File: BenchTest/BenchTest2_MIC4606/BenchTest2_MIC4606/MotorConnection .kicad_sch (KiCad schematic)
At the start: 4 parts, among them J1 Conn_01x01_Socket, J3 Conn_01x01_Socket, J4 Conn_01x01_Socket, J5 Conn_01x01_Socket

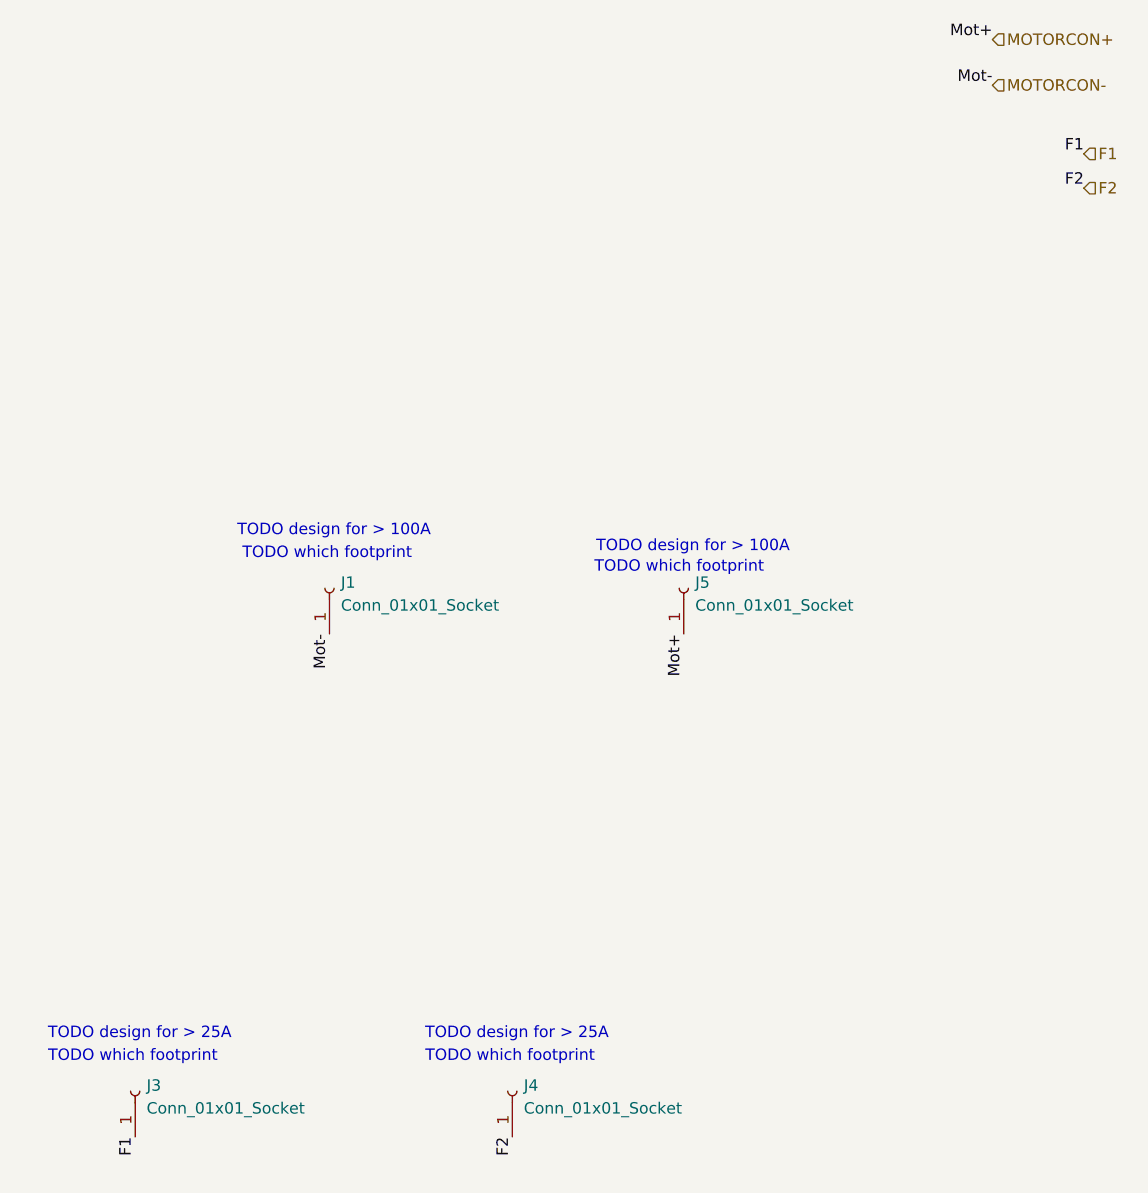
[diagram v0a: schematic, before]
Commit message: Assigned HP Footprints
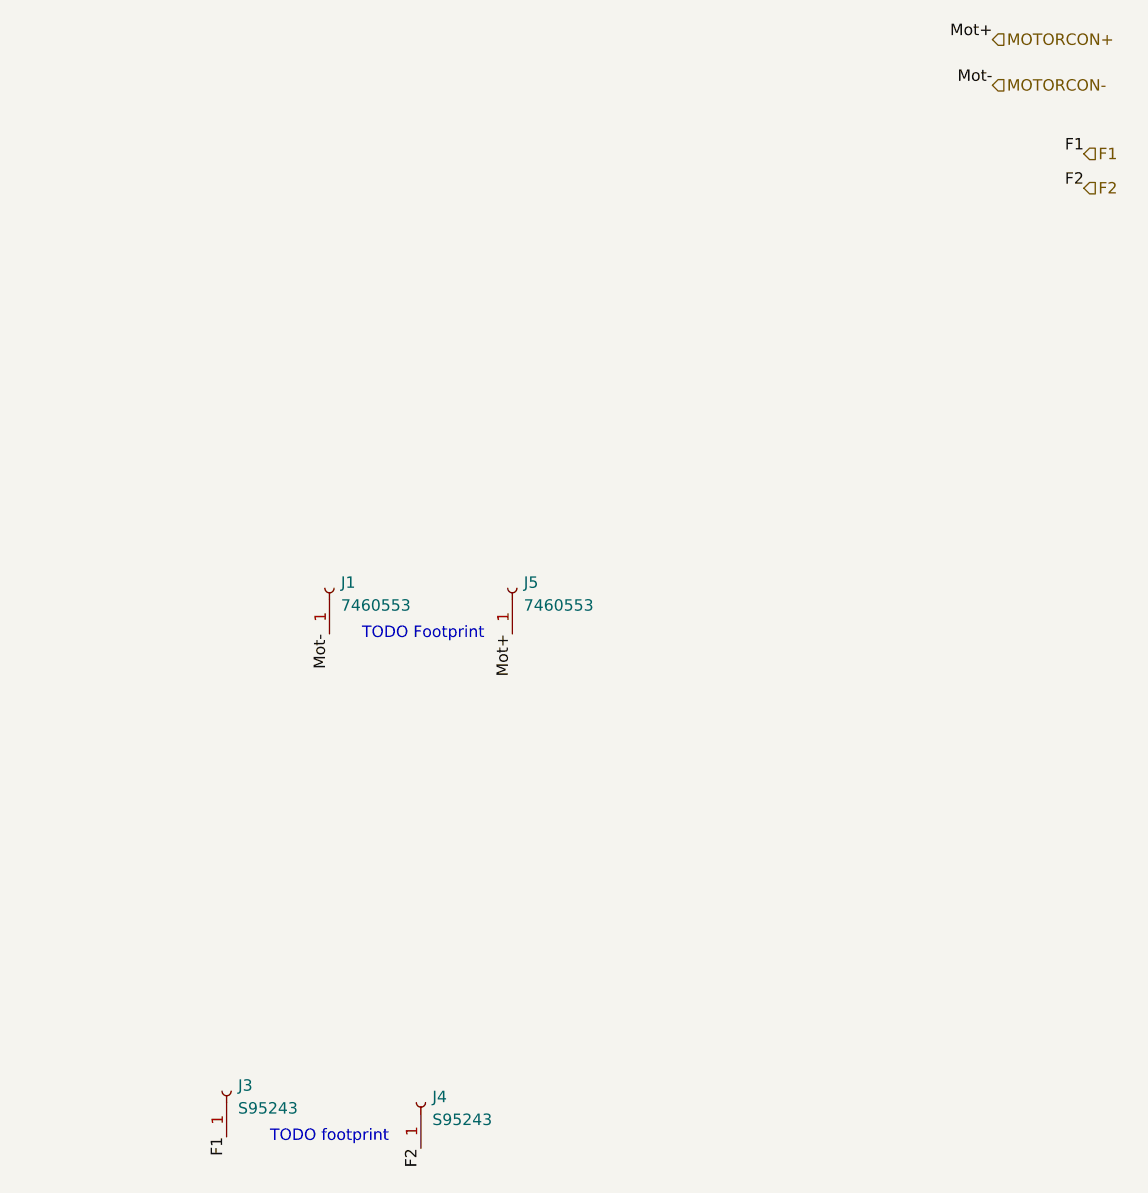
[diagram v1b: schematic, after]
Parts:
- J1, J5: value Conn_01x01_Socket -> 7460553
- J3, J4: value Conn_01x01_Socket -> S95243
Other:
- note added: "TODO Footprint"
- note added: "TODO footprint"
- note removed: "TODO design for > 100A"
- note removed: "TODO design for > 25A"
- note removed: "TODO which footprint"
- moved on the sheet: J3, J4, J5
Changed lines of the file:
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@@
 	(generator_version "9.0")
 	(paper "A4")
-	(text "TODO which footprint"
-		(exclude_from_sim no)
-		(at 173.736 132.08 0)
-		(effects
-			(font
-				(size 1.27 1.27)
-			)
-		)
-	)
-	(text "TODO which footprint"
-		(exclude_from_sim no)
-		(at 195.326 76.2 0)
-		(effects
-			(font
-				(size 1.27 1.27)
-			)
-		)
-	)
-	(text "TODO which footprint"
-		(exclude_from_sim no)
-		(at 234.442 77.724 0)
-		(effects
-			(font
-				(size 1.27 1.27)
-			)
-		)
-	)
-	(text "TODO design for > 100A"
-		(exclude_from_sim no)
-		(at 235.966 75.438 0)
-		(effects
-			(font
-				(size 1.27 1.27)
-			)
-		)
-	)
-	(text "TODO which footprint"
-		(exclude_from_sim no)
-		(at 215.646 132.08 0)
-		(effects
-			(font
-				(size 1.27 1.27)
-			)
-		)
-	)
-	(text "TODO design for > 100A"
-		(exclude_from_sim no)
-		(at 196.088 73.66 0)
-		(effects
-			(font
-				(size 1.27 1.27)
-			)
-		)
-	)
-	(text "TODO design for > 25A"
-		(exclude_from_sim no)
-		(at 216.408 129.54 0)
-		(effects
-			(font
-				(size 1.27 1.27)
-			)
-		)
-	)
-	(text "TODO design for > 25A"
-		(exclude_from_sim no)
-		(at 174.498 129.54 0)
+	(text "TODO Footprint"
+		(exclude_from_sim no)
+		(at 205.994 85.09 0)
+		(effects
+			(font
+				(size 1.27 1.27)
+			)
+		)
+	)
+	(text "TODO footprint"
+		(exclude_from_sim no)
+		(at 195.58 140.97 0)
 		(effects
 			(font
@@
 	)
 	(label "Mot+"
-		(at 234.95 85.09 270)
+		(at 215.9 85.09 270)
 		(effects
 			(font
@@
 	)
 	(label "F1"
-		(at 173.99 140.97 270)
+		(at 184.15 140.97 270)
 		(effects
 			(font
@@
 	)
 	(label "F2"
-		(at 215.9 140.97 270)
+		(at 205.74 142.24 270)
 		(effects
 			(font
@@
 			)
 		)
-		(property "Value" "Conn_01x01_Socket"
+		(property "Value" "7460553"
 			(at 196.85 81.9149 90)
 			(effects
@@
 			)
 		)
-		(property "Description" "Generic connector, single row, 01x01, script generated"
+		(property "Description" "7460553"
 			(at 195.58 80.01 0)
 			(effects
@@
 	(symbol
 		(lib_id "Connector:Conn_01x01_Socket")
-		(at 173.99 135.89 90)
+		(at 184.15 135.89 90)
 		(unit 1)
 		(exclude_from_sim no)
@@
 		(fields_autoplaced yes)
 		(property "Reference" "J3"
-			(at 175.26 135.2549 90)
-			(effects
-				(font
-					(size 1.27 1.27)
-				)
-				(justify right)
-			)
-		)
-		(property "Value" "Conn_01x01_Socket"
-			(at 175.26 137.7949 90)
+			(at 185.42 135.2549 90)
+			(effects
+				(font
+					(size 1.27 1.27)
+				)
+				(justify right)
+			)
+		)
+		(property "Value" "S95243"
+			(at 185.42 137.7949 90)
 			(effects
 				(font
@@
 		)
 		(property "Footprint" ""
-			(at 173.99 135.89 0)
+			(at 184.15 135.89 0)
 			(effects
 				(font
@@
 		)
 		(property "Datasheet" "~"
-			(at 173.99 135.89 0)
-			(effects
-				(font
-					(size 1.27 1.27)
-				)
-				(hide yes)
-			)
-		)
-		(property "Description" "Generic connector, single row, 01x01, script generated"
-			(at 173.99 135.89 0)
+			(at 184.15 135.89 0)
+			(effects
+				(font
+					(size 1.27 1.27)
+				)
+				(hide yes)
+			)
+		)
+		(property "Description" "S95243"
+			(at 184.15 135.89 0)
 			(effects
 				(font
@@
 	(symbol
 		(lib_id "Connector:Conn_01x01_Socket")
-		(at 234.95 80.01 90)
+		(at 215.9 80.01 90)
 		(unit 1)
 		(exclude_from_sim no)
@@
 		(fields_autoplaced yes)
 		(property "Reference" "J5"
-			(at 236.22 79.3749 90)
-			(effects
-				(font
-					(size 1.27 1.27)
-				)
-				(justify right)
-			)
-		)
-		(property "Value" "Conn_01x01_Socket"
-			(at 236.22 81.9149 90)
+			(at 217.17 79.3749 90)
+			(effects
+				(font
+					(size 1.27 1.27)
+				)
+				(justify right)
+			)
+		)
+		(property "Value" "7460553"
+			(at 217.17 81.9149 90)
 			(effects
 				(font
@@
 		)
 		(property "Footprint" ""
-			(at 234.95 80.01 0)
+			(at 215.9 80.01 0)
 			(effects
 				(font
@@
 		)
 		(property "Datasheet" "~"
-			(at 234.95 80.01 0)
-			(effects
-				(font
-					(size 1.27 1.27)
-				)
-				(hide yes)
-			)
-		)
-		(property "Description" "Generic connector, single row, 01x01, script generated"
-			(at 234.95 80.01 0)
+			(at 215.9 80.01 0)
+			(effects
+				(font
+					(size 1.27 1.27)
+				)
+				(hide yes)
+			)
+		)
+		(property "Description" "7460553"
+			(at 215.9 80.01 0)
 			(effects
 				(font
@@
 	(symbol
 		(lib_id "Connector:Conn_01x01_Socket")
-		(at 215.9 135.89 90)
+		(at 205.74 137.16 90)
 		(unit 1)
 		(exclude_from_sim no)
@@
 		(fields_autoplaced yes)
 		(property "Reference" "J4"
-			(at 217.17 135.2549 90)
-			(effects
-				(font
-					(size 1.27 1.27)
-				)
-				(justify right)
-			)
-		)
-		(property "Value" "Conn_01x01_Socket"
-			(at 217.17 137.7949 90)
+			(at 207.01 136.5249 90)
+			(effects
+				(font
+					(size 1.27 1.27)
+				)
+				(justify right)
+			)
+		)
+		(property "Value" "S95243"
+			(at 207.01 139.0649 90)
 			(effects
 				(font
@@
 		)
 		(property "Footprint" ""
-			(at 215.9 135.89 0)
+			(at 205.74 137.16 0)
 			(effects
 				(font
@@
 		)
 		(property "Datasheet" "~"
-			(at 215.9 135.89 0)
-			(effects
-				(font
-					(size 1.27 1.27)
-				)
-				(hide yes)
-			)
-		)
-		(property "Description" "Generic connector, single row, 01x01, script generated"
-			(at 215.9 135.89 0)
-			(effects
-				(font
+			(at 205.74 137.16 0)
+			(effects
+				(font
+					(size 1.27 1.27)
+				)
+				(hide yes)
+			)
+		)
+		(property "Description" "S95243"
+			(at 205.74 137.16 0)
+			(effects
+				(font
